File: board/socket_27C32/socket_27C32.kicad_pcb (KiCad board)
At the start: 2 copper layers, 17.8 x 35.6 mm, 2 parts, among them J1 Adapter

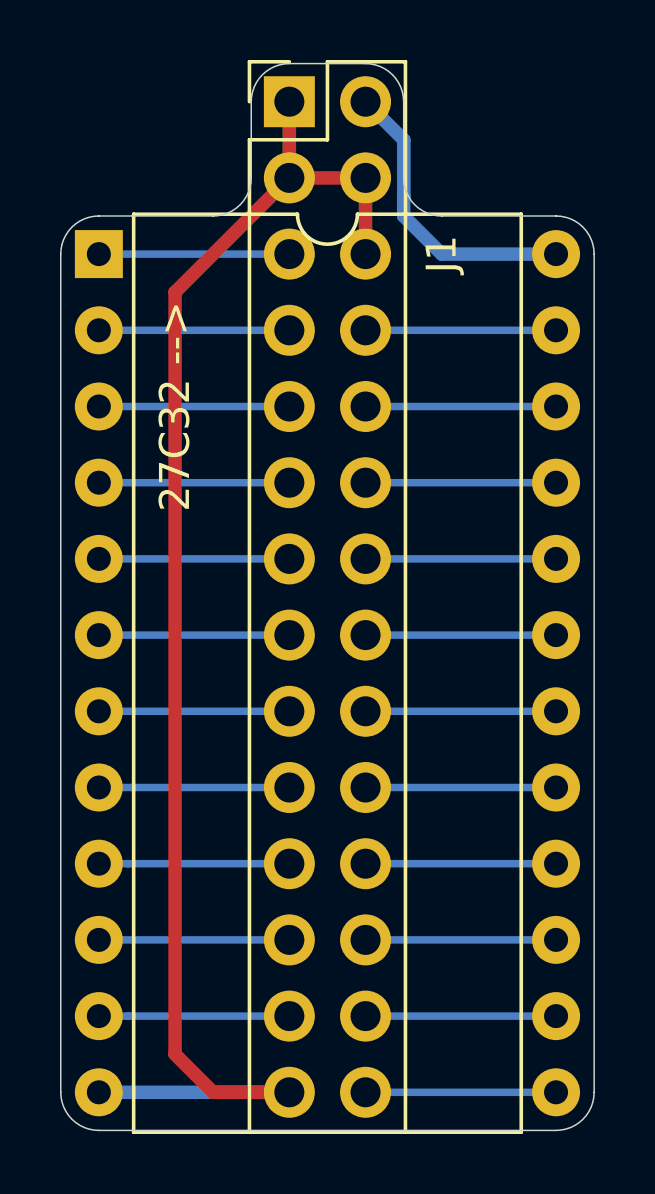
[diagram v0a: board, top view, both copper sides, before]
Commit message: Add 27C400/16 socket
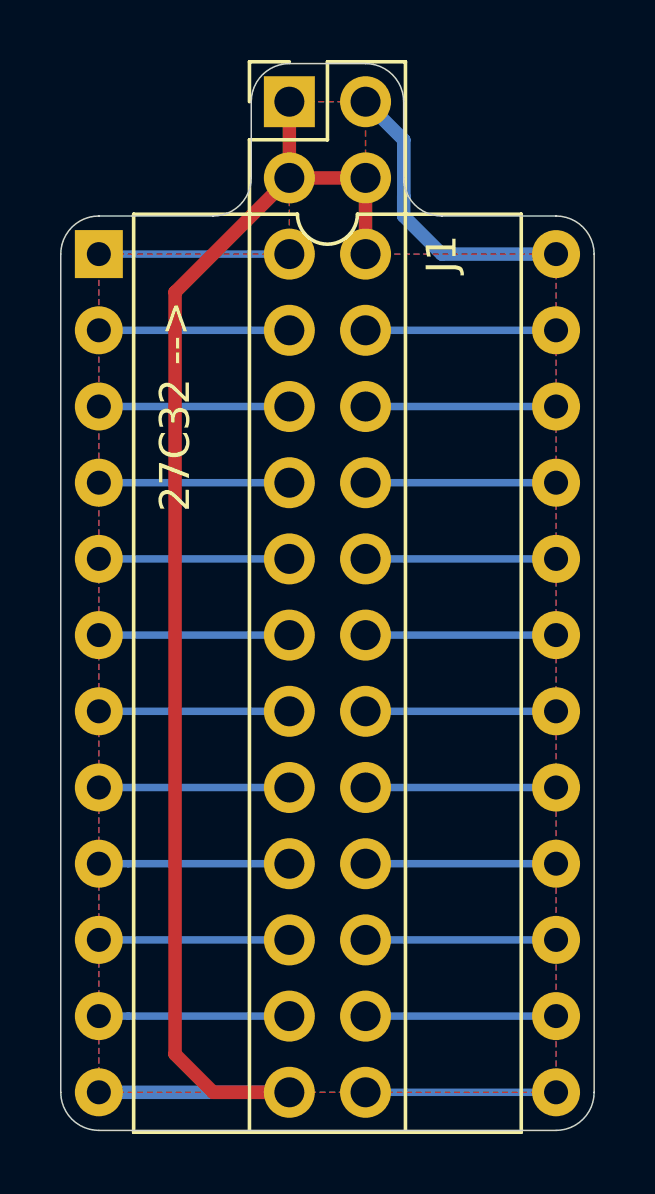
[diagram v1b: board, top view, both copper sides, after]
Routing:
- added copper zone on B.Cu, net GND
- added copper zone on F.Cu, net GND
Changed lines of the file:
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@@
       (effects (font (size 1 1) (thickness 0.15)))
     )
+    (fp_line (start 16.3 -1.55) (end -1.05 -1.55) (layer F.CrtYd) (width 0.05))
+    (fp_line (start 16.3 29.5) (end 16.3 -1.55) (layer F.CrtYd) (width 0.05))
+    (fp_line (start -1.05 29.5) (end 16.3 29.5) (layer F.CrtYd) (width 0.05))
+    (fp_line (start -1.05 -1.55) (end -1.05 29.5) (layer F.CrtYd) (width 0.05))
+    (fp_line (start 14.08 -1.33) (end 8.62 -1.33) (layer F.SilkS) (width 0.12))
+    (fp_line (start 14.08 29.27) (end 14.08 -1.33) (layer F.SilkS) (width 0.12))
+    (fp_line (start 1.16 29.27) (end 14.08 29.27) (layer F.SilkS) (width 0.12))
+    (fp_line (start 1.16 -1.33) (end 1.16 29.27) (layer F.SilkS) (width 0.12))
+    (fp_line (start 6.62 -1.33) (end 1.16 -1.33) (layer F.SilkS) (width 0.12))
+    (fp_line (start 0.255 -0.27) (end 1.255 -1.27) (layer F.Fab) (width 0.1))
+    (fp_line (start 0.255 29.21) (end 0.255 -0.27) (layer F.Fab) (width 0.1))
+    (fp_line (start 14.985 29.21) (end 0.255 29.21) (layer F.Fab) (width 0.1))
+    (fp_line (start 14.985 -1.27) (end 14.985 29.21) (layer F.Fab) (width 0.1))
+    (fp_line (start 1.255 -1.27) (end 14.985 -1.27) (layer F.Fab) (width 0.1))
     (fp_text user %R (at 7.62 13.97) (layer F.Fab)
       (effects (font (size 1 1) (thickness 0.15)))
     )
     (fp_arc (start 7.62 -1.33) (end 6.62 -1.33) (angle -180) (layer F.SilkS) (width 0.12))
-    (fp_line (start 1.255 -1.27) (end 14.985 -1.27) (layer F.Fab) (width 0.1))
-    (fp_line (start 14.985 -1.27) (end 14.985 29.21) (layer F.Fab) (width 0.1))
-    (fp_line (start 14.985 29.21) (end 0.255 29.21) (layer F.Fab) (width 0.1))
-    (fp_line (start 0.255 29.21) (end 0.255 -0.27) (layer F.Fab) (width 0.1))
-    (fp_line (start 0.255 -0.27) (end 1.255 -1.27) (layer F.Fab) (width 0.1))
-    (fp_line (start 6.62 -1.33) (end 1.16 -1.33) (layer F.SilkS) (width 0.12))
-    (fp_line (start 1.16 -1.33) (end 1.16 29.27) (layer F.SilkS) (width 0.12))
-    (fp_line (start 1.16 29.27) (end 14.08 29.27) (layer F.SilkS) (width 0.12))
-    (fp_line (start 14.08 29.27) (end 14.08 -1.33) (layer F.SilkS) (width 0.12))
-    (fp_line (start 14.08 -1.33) (end 8.62 -1.33) (layer F.SilkS) (width 0.12))
-    (fp_line (start -1.05 -1.55) (end -1.05 29.5) (layer F.CrtYd) (width 0.05))
-    (fp_line (start -1.05 29.5) (end 16.3 29.5) (layer F.CrtYd) (width 0.05))
-    (fp_line (start 16.3 29.5) (end 16.3 -1.55) (layer F.CrtYd) (width 0.05))
-    (fp_line (start 16.3 -1.55) (end -1.05 -1.55) (layer F.CrtYd) (width 0.05))
     (pad 24 thru_hole oval (at 15.24 0) (size 1.6 1.6) (drill 0.8) (layers *.Cu *.Mask)
       (net 24 /VCC_EXT))
@@
       (effects (font (size 1 1) (thickness 0.15)))
     )
+    (fp_line (start 0 -1.27) (end 3.81 -1.27) (layer F.Fab) (width 0.1))
+    (fp_line (start 3.81 -1.27) (end 3.81 34.29) (layer F.Fab) (width 0.1))
+    (fp_line (start 3.81 34.29) (end -1.27 34.29) (layer F.Fab) (width 0.1))
+    (fp_line (start -1.27 34.29) (end -1.27 0) (layer F.Fab) (width 0.1))
+    (fp_line (start -1.27 0) (end 0 -1.27) (layer F.Fab) (width 0.1))
+    (fp_line (start -1.33 34.35) (end 3.87 34.35) (layer F.SilkS) (width 0.12))
+    (fp_line (start -1.33 1.27) (end -1.33 34.35) (layer F.SilkS) (width 0.12))
+    (fp_line (start 3.87 -1.33) (end 3.87 34.35) (layer F.SilkS) (width 0.12))
+    (fp_line (start -1.33 1.27) (end 1.27 1.27) (layer F.SilkS) (width 0.12))
+    (fp_line (start 1.27 1.27) (end 1.27 -1.33) (layer F.SilkS) (width 0.12))
+    (fp_line (start 1.27 -1.33) (end 3.87 -1.33) (layer F.SilkS) (width 0.12))
+    (fp_line (start -1.33 0) (end -1.33 -1.33) (layer F.SilkS) (width 0.12))
+    (fp_line (start -1.33 -1.33) (end 0 -1.33) (layer F.SilkS) (width 0.12))
+    (fp_line (start -1.8 -1.8) (end -1.8 34.8) (layer F.CrtYd) (width 0.05))
+    (fp_line (start -1.8 34.8) (end 4.35 34.8) (layer F.CrtYd) (width 0.05))
+    (fp_line (start 4.35 34.8) (end 4.35 -1.8) (layer F.CrtYd) (width 0.05))
     (fp_line (start 4.35 -1.8) (end -1.8 -1.8) (layer F.CrtYd) (width 0.05))
-    (fp_line (start 4.35 34.8) (end 4.35 -1.8) (layer F.CrtYd) (width 0.05))
-    (fp_line (start -1.8 34.8) (end 4.35 34.8) (layer F.CrtYd) (width 0.05))
-    (fp_line (start -1.8 -1.8) (end -1.8 34.8) (layer F.CrtYd) (width 0.05))
-    (fp_line (start -1.33 -1.33) (end 0 -1.33) (layer F.SilkS) (width 0.12))
-    (fp_line (start -1.33 0) (end -1.33 -1.33) (layer F.SilkS) (width 0.12))
-    (fp_line (start 1.27 -1.33) (end 3.87 -1.33) (layer F.SilkS) (width 0.12))
-    (fp_line (start 1.27 1.27) (end 1.27 -1.33) (layer F.SilkS) (width 0.12))
-    (fp_line (start -1.33 1.27) (end 1.27 1.27) (layer F.SilkS) (width 0.12))
-    (fp_line (start 3.87 -1.33) (end 3.87 34.35) (layer F.SilkS) (width 0.12))
-    (fp_line (start -1.33 1.27) (end -1.33 34.35) (layer F.SilkS) (width 0.12))
-    (fp_line (start -1.33 34.35) (end 3.87 34.35) (layer F.SilkS) (width 0.12))
-    (fp_line (start -1.27 0) (end 0 -1.27) (layer F.Fab) (width 0.1))
-    (fp_line (start -1.27 34.29) (end -1.27 0) (layer F.Fab) (width 0.1))
-    (fp_line (start 3.81 34.29) (end -1.27 34.29) (layer F.Fab) (width 0.1))
-    (fp_line (start 3.81 -1.27) (end 3.81 34.29) (layer F.Fab) (width 0.1))
-    (fp_line (start 0 -1.27) (end 3.81 -1.27) (layer F.Fab) (width 0.1))
     (fp_text user %R (at 1.27 16.51 90) (layer F.Fab)
       (effects (font (size 1 1) (thickness 0.15)))
@@
   (segment (start 129.54 77.47) (end 129.54 76.817002) (width 0.45) (layer B.Cu) (net 24))
   (segment (start 129.545001 74.935001) (end 128.27 73.66) (width 0.45) (layer B.Cu) (net 24))
+  (zone (net 2) (net_name GND) (layer B.Cu) (hatch edge 0.508)
+    (connect_pads (clearance 0.508))
+    (min_thickness 0.254)
+    (fill yes (arc_segments 32) (thermal_gap 0.508) (thermal_bridge_width 0.508))
+    (polygon
+      (pts
+        (xy 128.27 78.74) (xy 134.62 78.74) (xy 134.62 106.68) (xy 119.38 106.68) (xy 119.38 78.74)
+        (xy 125.73 78.74) (xy 125.73 73.66) (xy 128.27 73.66)
+      )
+    )
+  )
+  (zone (net 2) (net_name GND) (layer F.Cu) (hatch edge 0.508)
+    (connect_pads (clearance 0.508))
+    (min_thickness 0.254)
+    (fill yes (arc_segments 32) (thermal_gap 0.508) (thermal_bridge_width 0.508))
+    (polygon
+      (pts
+        (xy 128.27 78.74) (xy 134.62 78.74) (xy 134.62 106.68) (xy 119.38 106.68) (xy 119.38 78.74)
+        (xy 125.73 78.74) (xy 125.73 73.66) (xy 128.27 73.66)
+      )
+    )
+  )
 )
